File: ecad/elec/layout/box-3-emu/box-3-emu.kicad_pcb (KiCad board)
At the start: 2 copper layers, 72.5 x 63.9 mm, 75 parts

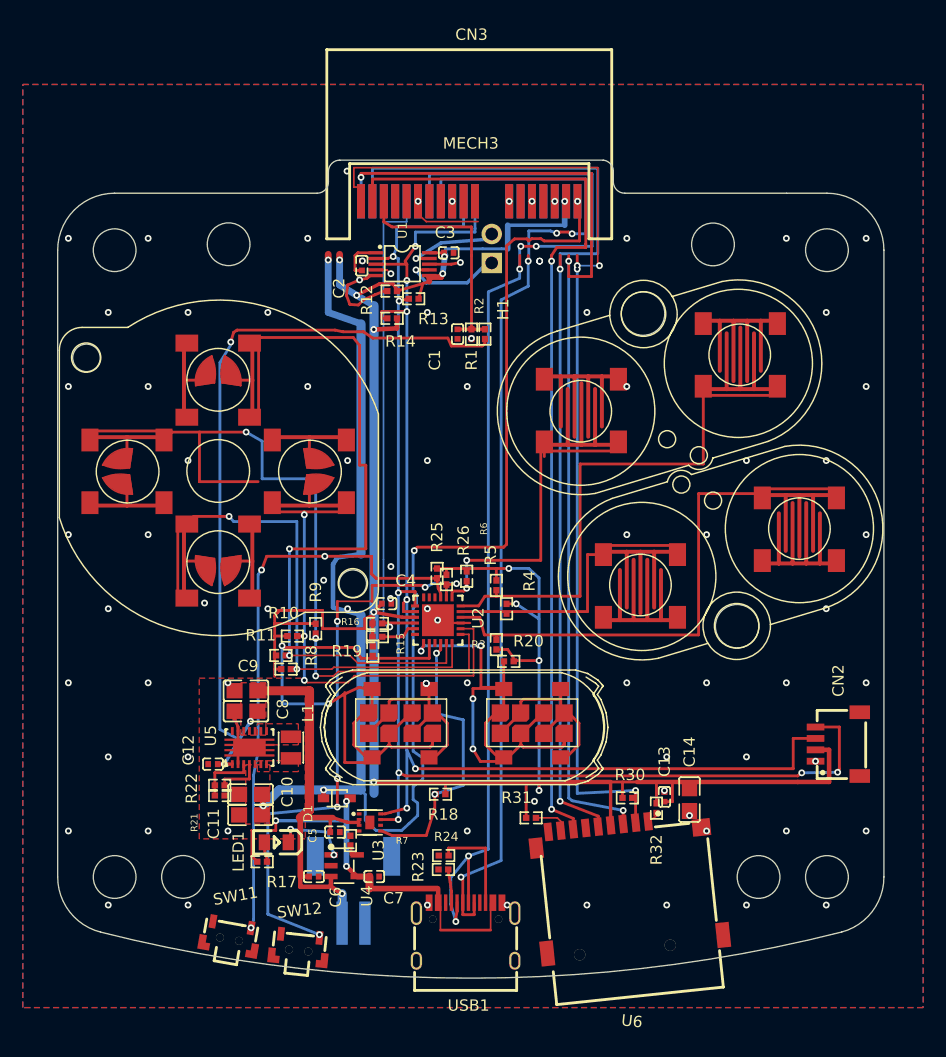
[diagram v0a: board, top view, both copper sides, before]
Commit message: fix(ecad): eliminate via-in-pad instances; add DRC rule to catch them
JLCPCB's standard process wicks solder from reflowed pads into via
barrels, so via-in-pad needs the paid filled/capped process. Relocate
every offending via out of its pad with a short connecting trace:
21 shared instances (bypass caps, pullups, switches, USB shell, SD
shell, qwiic, charger STAT, divider) plus the box-emu J3 and box-3
CN3 power-finger vias. C13 flips 180 so its ground pad escapes south
to C14; R11 shifts 0.35mm west to free the up-net junction; the
DRV2605 REG (hv) wrap reroutes west to make room beside C2.

A physical_hole_clearance rule in each board's .kicad_dru now flags
any via hole within 0.1mm of an SMD pad, with documented exceptions:
the AW9523 thermal pad (stitching vias are standard practice), gnd
card-edge fingers (no paste/reflow; dimple on redundant ground mating
surfaces is acceptable), and C3's 85um same-net corner graze (any
relocation severs the only ground-pour channel through that neck).

Ground-pour integrity reverified after the churn: several relocations
had orphaned the central gnd island (the old SW9 and C2 vias doubled
as pour stitches); connectivity now reports 0 unconnected on all
three boards by both kicad-cli DRC and pcbnew's engine.

Co-Authored-By: Claude Fable 5 <noreply@anthropic.com>
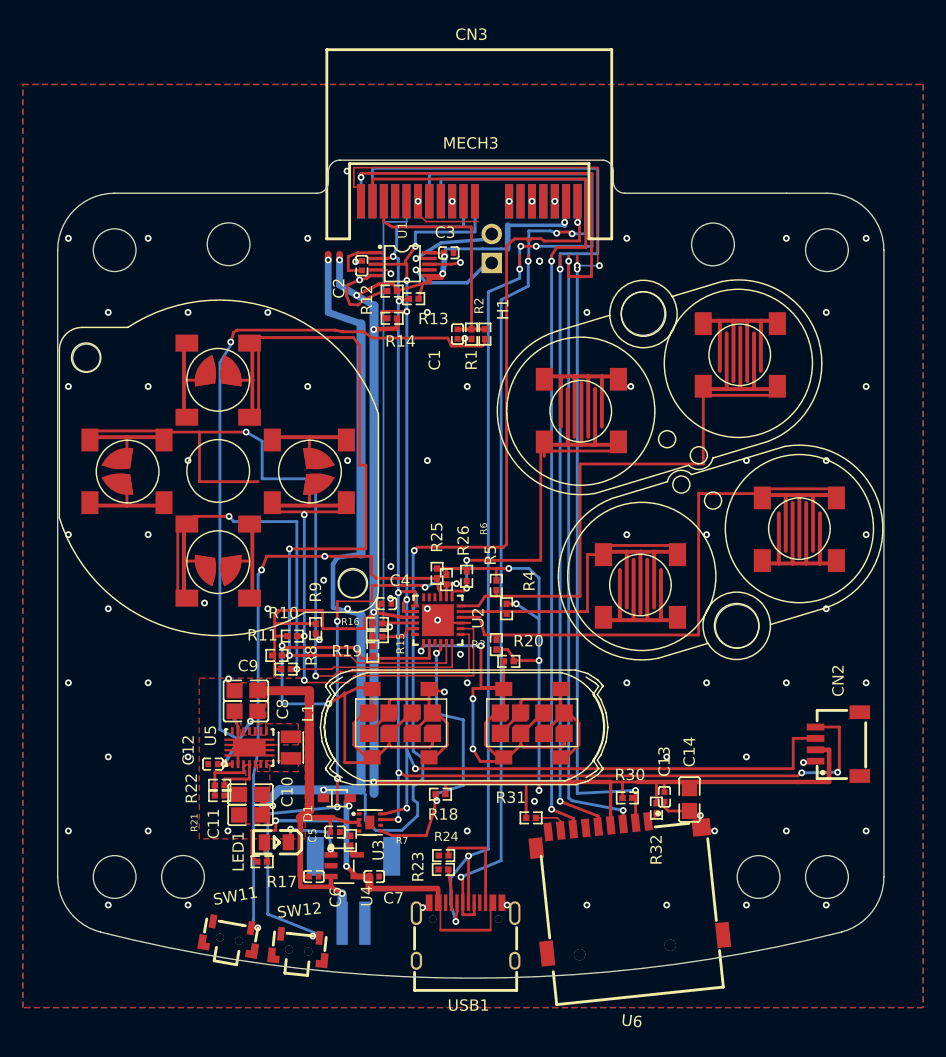
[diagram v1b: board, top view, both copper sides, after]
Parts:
- moved R11 0.35 mm to (133.6, 117.4)
- turned C13 to -90 degrees
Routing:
- net gnd: track 14.0 -> 23.8 mm, vias 82 -> 81
- net vcc_5v: track 143.8 -> 146.2 mm
- net nALRT: track 24.3 -> 25.8 mm
- net vcc_3v3: track 203.7 -> 202.2 mm
- net vol_down: track 50.1 -> 51.3 mm
- net hv: track 3.21 -> 4.26 mm
- net up: track 67.6 -> 68.3 mm
- net vol_up: track 50.9 -> 51.5 mm
- net STAT: track 6.52 -> 7.10 mm

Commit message: feat(ecad): add battery-drain debug provisions (test points + boost EN isolation)
- New TESTPOINT part (1.5mm bare-copper probe pad, no BOM line):
  TP1=5V, TP2=boost EN, TP3=GND, TP4=VBAT, placed in the open field
  south of the TPS63020 on all three boards.
- boost EN is now fed through R27 (10k 0402) from VBAT instead of a
  hard copper tie: lifting/probing TP2 (or grounding it through the
  10k) shuts the boost down, letting battery-only standby current be
  split into boost IQ vs downstream-5V leakage during bring-up.
- EN routed as 0.14/0.15mm trace through the C8/C9 pad slots; the
  displaced vbat F-B transfer via relocated south with a new B return
  to the trunk junction.
- DRC baselines unchanged (265/266/271), 0 unconnected everywhere.

Co-Authored-By: Claude Fable 5 <noreply@anthropic.com>
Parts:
- added R27: 10kΩ ±5%, UNI_ROYAL_0402WGF1002TCE:R0402, F.Cu at (131.4, 119.3)
- added TP1: , TESTPOINT:TESTPOINT, F.Cu at (134.3, 130.6)
- added TP2: , TESTPOINT:TESTPOINT, F.Cu at (129.3, 117.7)
- added TP3: , TESTPOINT:TESTPOINT, F.Cu at (126.8, 126.9)
- added TP4: , TESTPOINT:TESTPOINT, F.Cu at (131.6, 117.9)
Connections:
- U5 pad 12: vbat -> boost_en
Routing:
- net vbat: track 102.6 -> 112.1 mm
- net boost_en: track 0.00 -> 7.01 mm
- net vcc_5v: track 146.2 -> 147.3 mm

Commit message: feat: switch uSD to native SDMMC; provision 4-bit on the BOX carrier
Firmware: replace the SDSPI host (which ran at the 20MHz default) with
the S3's SDMMC host routed through the GPIO matrix on the same lines
(CLK=12, CMD=11, DAT0=13), 1-bit wide at 40MHz high-speed -- roughly
3-4x the read throughput on every existing board, and SPI3 is freed.
DAT3 is parked high by its on-board pullup, which also keeps the card
out of SPI mode; CMD/DAT0 use the internal pullups.

ECAD (next rev): the socket module now exposes DAT1/DAT2, and the BOX
carrier wires them to PMOD fingers io9/io44 for 4-bit SDMMC (io44 is
U0RXD, an input at boot, so it is safe as an SD line; io43/U0TXD would
drive ROM boot logs into the card). Routed as B-layer columns at
x26.3/x27.65 with F-layer pocket escapes past the B-side vcc/INTN
fences and south corridors under the socket; DRC baselines unchanged,
0 unconnected on all three boards.

The BOX-3 carrier stays 1-bit: its dock tab has 1.24mm of fan-out band
per side against the 1.40mm five lanes would need even restacked at
0.15mm, and every candidate spare finger except A11 is boxed in by the
battery/gnd/INTN/SCL escapes (SD has no 2-bit mode, so one line is no
use). Documented in box-3-emu.ato.

Co-Authored-By: Claude Fable 5 <noreply@anthropic.com>
Claude-Session: https://claude.ai/code/session_014M3Ezo5uTqn1QXTWTC6fAf
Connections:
- CN3 pad A4: io9 -> conn-io9
- CN3 pad B4: io44 -> conn-io44
- R31 pad 2: 8 -> io9
- R32 pad 2: box.uSD-1 -> io44
- U6 pad 1: box.uSD-1 -> io44
- U6 pad 8: 8 -> io9
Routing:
- net io9: track 0.00 -> 3.12 mm
- net 8: track 3.12 -> 0.00 mm
- net io44: track 0.00 -> 1.13 mm
- net box.uSD-1: track 1.13 -> 0.00 mm

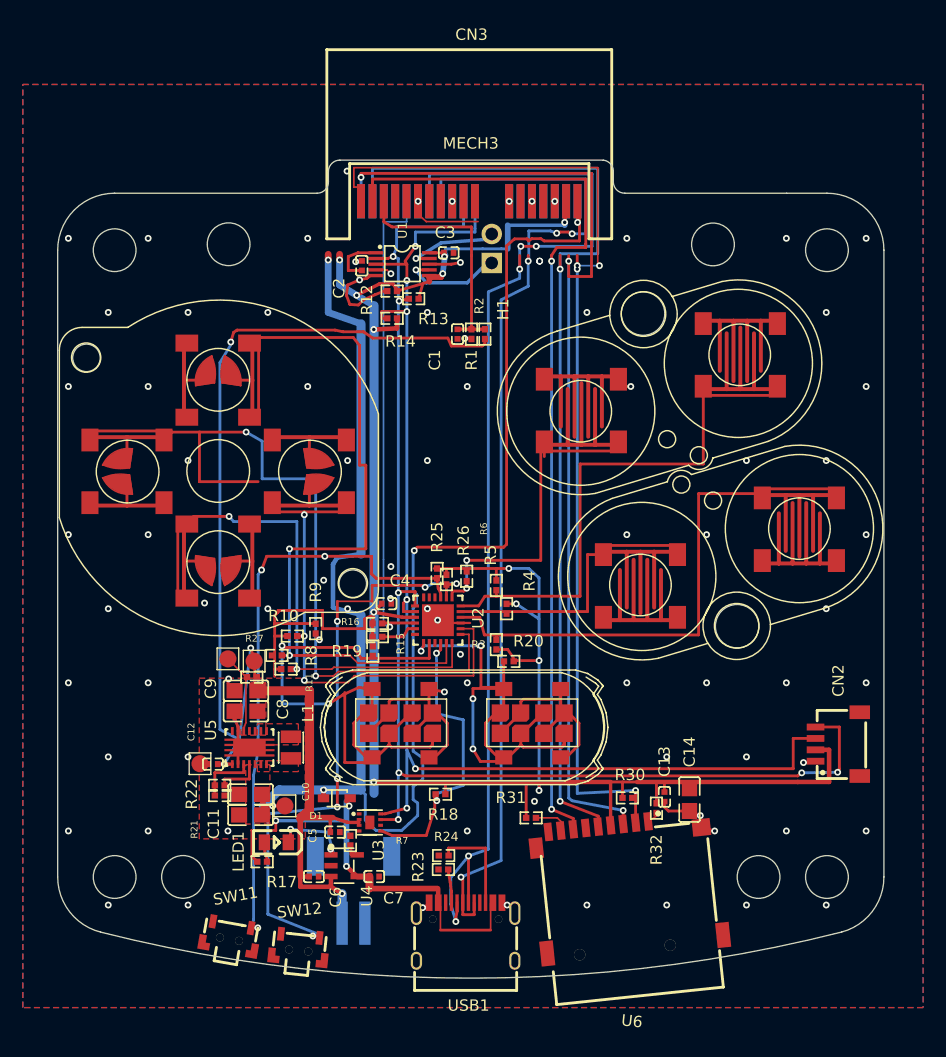
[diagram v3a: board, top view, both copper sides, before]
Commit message: fix(ecad): open up cramped parts around the uSD socket and TPS63020
Layout review pass (programmatic courtyard + pad-to-pad sweep, and
KiCad DRC at warning severity):
- C14 (22uF SD bulk cap): its gnd pad was merged into the uSD socket
  shell pad (<0.1mm). Rotated 90 deg and shifted east so the pad sits
  0.9mm off the shell; it cannot move north (SCL trace at y48.67).
- R32 (DAT2 pullup): pad was 0.03mm from socket pad 1 and 0.16mm from
  C13 (one of the accepted DRC clearance hits). Re-oriented horizontal
  in the free slot between R30 and C13; all gaps now >=0.3mm, and the
  clearance-violation count drops by one on every board.
- TP3 was touching C12's gnd pad; moved north of C12 on the tps_gnd
  pour, clear of the 0.1mm via-hole rule.
- R27/TP4/vbat via: R27 sat 0.25mm from C9's pads; raised it and TP4
  0.3-0.45mm, relocated the vbat layer-transfer via to keep its hole
  0.1mm from the TP4 pad.
- TESTPOINT footprint: silk square moved to F.Fab (it collided with
  neighbouring silk on every placement).
- Removed the duplicated gnd via at (5.35,3.5) on both variants
  (co-located holes) and the 1mm 3v3 artery tail past its junction via.

Schematic: header for the uSD block updated for SDMMC; firmware header
notes that io44 (DAT2 on the BOX carrier) is the default console's RX.
0 unconnected on all three boards; error baselines 264/265/270.

Co-Authored-By: Claude Fable 5.1 <noreply@anthropic.com>
Claude-Session: https://claude.ai/code/session_014M3Ezo5uTqn1QXTWTC6fAf
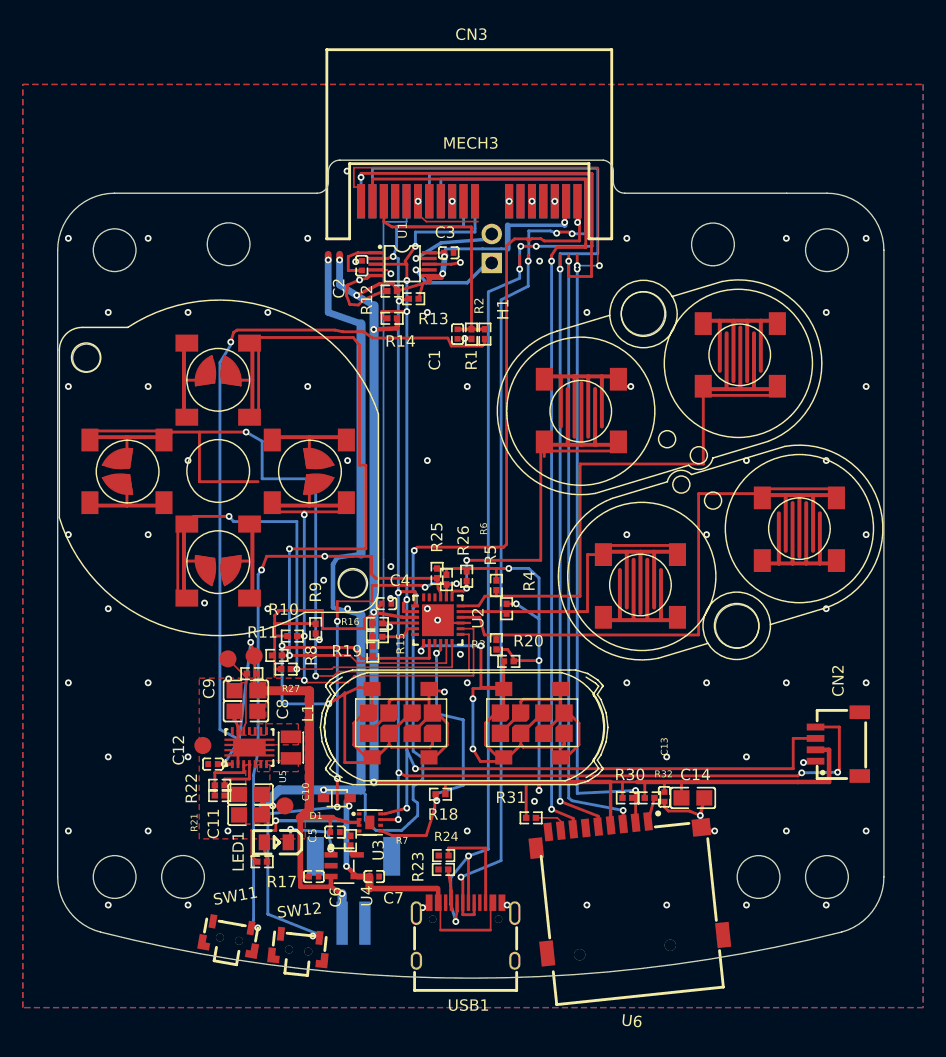
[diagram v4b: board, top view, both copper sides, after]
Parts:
- moved TP3 1.62 mm to (127.1, 125.3)
- moved R32 1.08 mm to (166.3, 129.9), turned to 0 degrees
- moved TP4 0.45 mm to (131.6, 117.5)
- moved C14 0.34 mm to (170.1, 129.9), turned to 0 degrees
- moved R27 0.30 mm to (131.4, 119.0)
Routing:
- net gnd: track 23.8 -> 25.0 mm, vias 81 -> 80
- net io44: track 1.13 -> 2.13 mm
- net vbat: track 112.1 -> 112.7 mm
